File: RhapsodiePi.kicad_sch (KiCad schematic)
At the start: 0 parts

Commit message: New i.mx6 Version
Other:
- note added: "MCIMX6Y2CVM08AB"

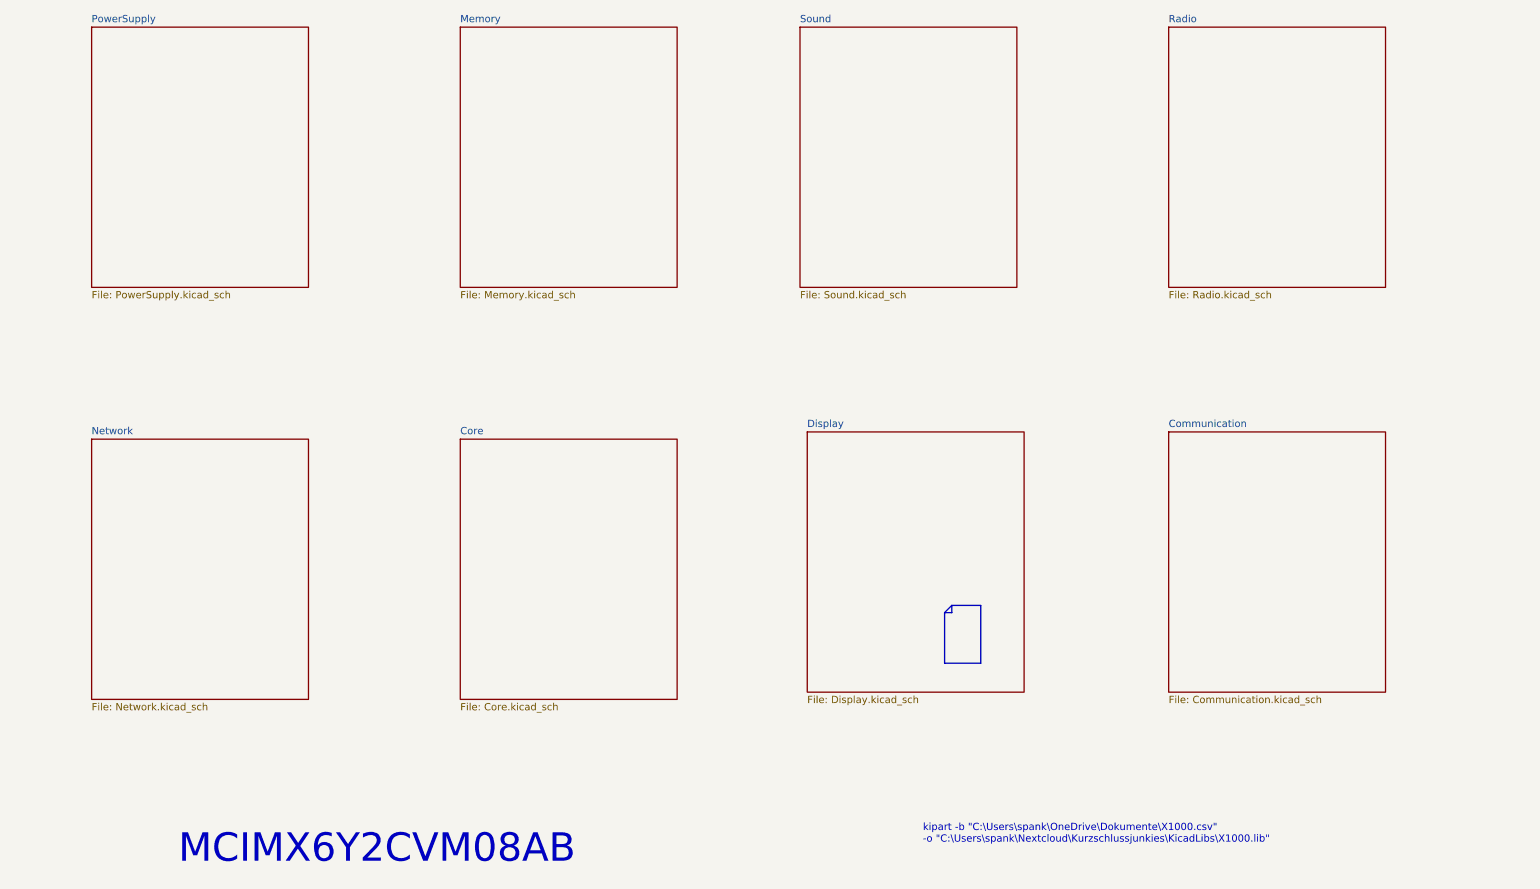
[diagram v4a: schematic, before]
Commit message: Display Update
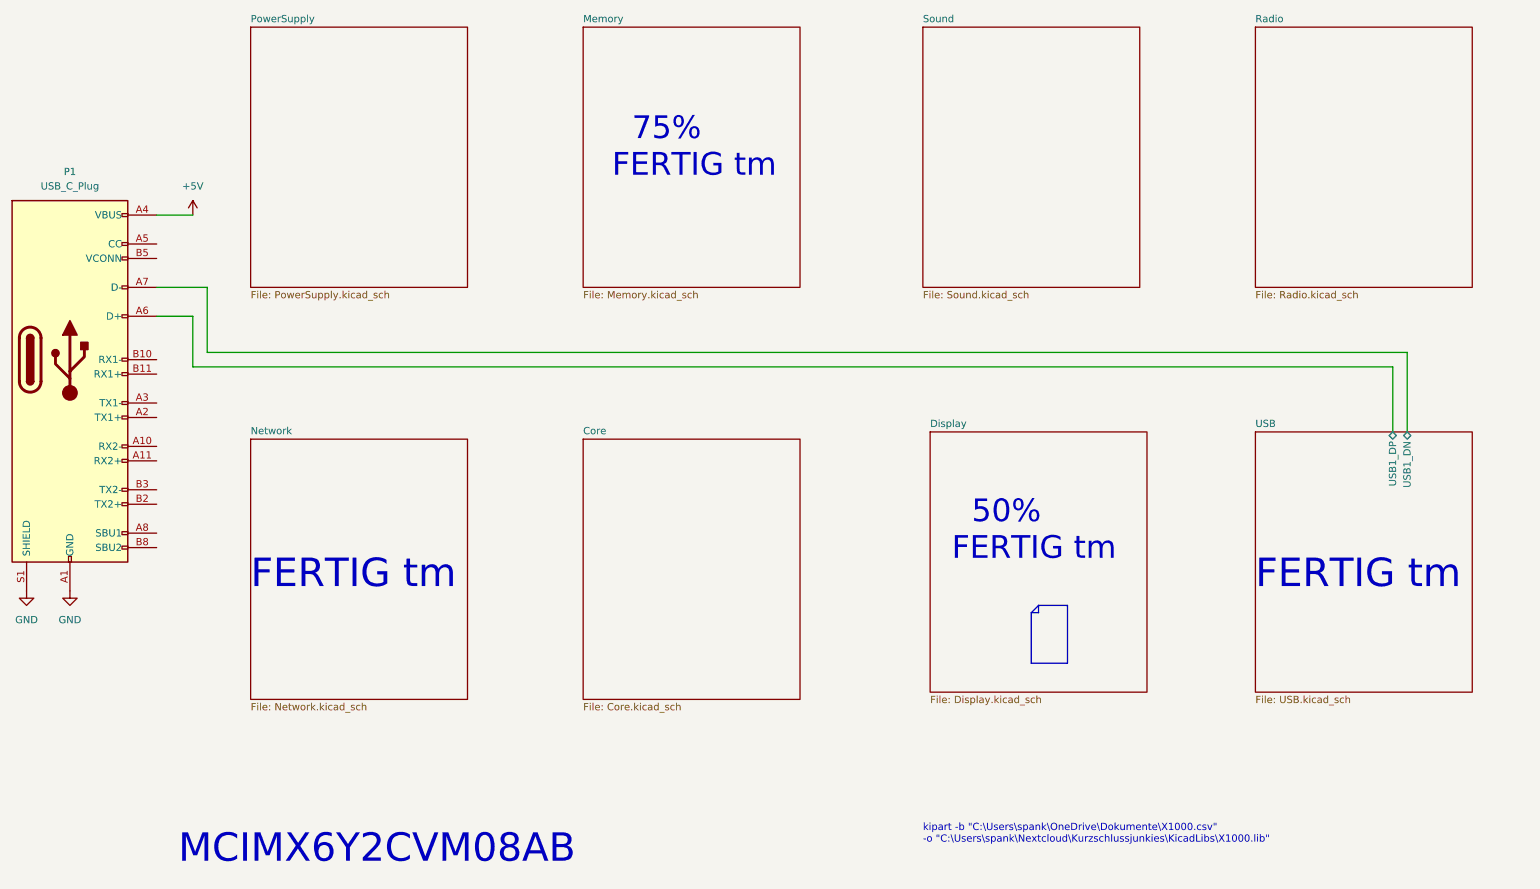
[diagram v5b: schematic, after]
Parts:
- added P1: USB_C_Plug, Connector_USB:USB_C_Receptacle_HRO_TYPE-C-31-M-12, symbol Connector:USB_C_Plug
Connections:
- new net +5V: P1.A4 (VBUS), P1.A9 (VBUS), P1.B4 (VBUS), P1.B9 (VBUS)
- new net GND: P1.A1 (GND), P1.A12 (GND), P1.B1 (GND), P1.B12 (GND), P1.S1 (SHIELD)
- new net USB/USB1_DN: P1.A7 (D-)
- new net USB/USB1_DP: P1.A6 (D+)
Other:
- sheet Communication renamed USB
- sheet USB: file Communication.kicad_sch -> USB.kicad_sch
- sheet USB ports: added USB1_DN, USB1_DP; removed none
- note added: "50% FERTIG tm"
- note added: "75% FERTIG tm"
- note added: "FERTIG tm"

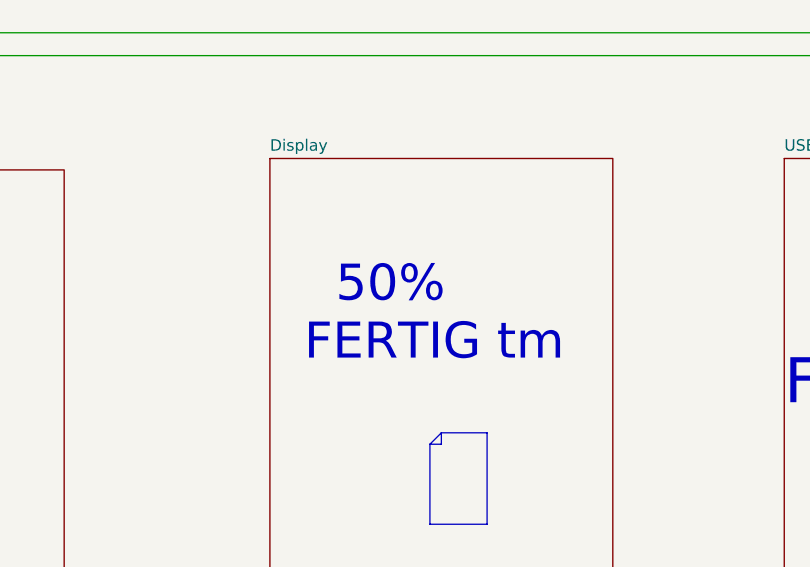
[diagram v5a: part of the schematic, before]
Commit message: update DDR
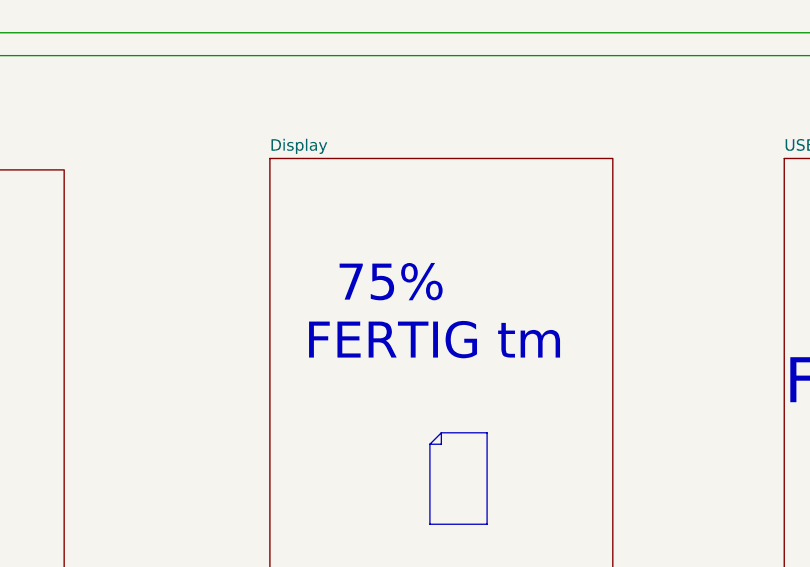
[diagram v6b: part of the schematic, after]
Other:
- note removed: "50% FERTIG tm"
